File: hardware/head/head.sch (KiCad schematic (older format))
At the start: 12 parts, among them J1 DB9_Male, J2 Stats_Button, J3 Flush_Button, J4 Brew_Button, J5 Temp_Ok, J6 Display, J7 HX711, J8 Rotary_Encoder, U1 Teensy4.0

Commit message: Update head unit
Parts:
- removed H1: MountingHole_Pad, MountingHole:MountingHole_2.5mm_Pad, symbol Mechanical:MountingHole_Pad
- removed J4: Brew_Button, Connector_PinHeader_2.54mm:PinHeader_1x02_P2.54mm_Vertical, symbol Connector:Conn_01x02_Male
- added C1, C13, C14, C15: 0.1uF, Capacitor_THT:C_Disc_D5.1mm_W3.2mm_P5.00mm, symbol Device:C
- added C10, C12, C4, C6, C7, C9: 1nF, Capacitor_THT:C_Disc_D5.1mm_W3.2mm_P5.00mm, symbol Device:C
- added C11, C5, C8: 10nF, Capacitor_THT:C_Disc_D5.1mm_W3.2mm_P5.00mm, symbol Device:C
- added C2: 150uF, Capacitor_THT:CP_Radial_D5.0mm_P2.00mm, symbol Device:CP
- added C3: 100uF, Capacitor_THT:CP_Radial_D5.0mm_P2.00mm, symbol Device:CP
- added D1: 1N5817, Diode_THT:D_DO-41_SOD81_P10.16mm_Horizontal, symbol Diode:1N5817
- added H3, H4: MountingHole_Pad, MountingHole:MountingHole_2.5mm_Pad, symbol Mechanical:MountingHole_Pad
- added J10: Pump_Active, Connector_PinHeader_2.54mm:PinHeader_1x02_P2.54mm_Vertical, symbol Connector:Conn_01x02_Male
- added J4: Brew_Button, Connector_PinHeader_2.54mm:PinHeader_1x04_P2.54mm_Vertical, symbol Connector:Conn_01x04_Male
- added J9: Heater_Active, Connector_PinHeader_2.54mm:PinHeader_1x02_P2.54mm_Vertical, symbol Connector:Conn_01x02_Male
- added L1: 22uH, Inductor_THT:L_Axial_L11.0mm_D4.5mm_P15.24mm_Horizontal_Fastron_MECC, symbol Device:L
- added Q1: IRF540N, Package_TO_SOT_THT:TO-220-3_Vertical, symbol Transistor_FET:IRF540N
- added R10, R5, R6, R7, R8, R9: 10k, Resistor_THT:R_Axial_DIN0204_L3.6mm_D1.6mm_P5.08mm_Horizontal, symbol Device:R
- added R11, R12: 400, Resistor_THT:R_Axial_DIN0204_L3.6mm_D1.6mm_P5.08mm_Horizontal, symbol Device:R
- added R13: 650, Resistor_THT:R_Axial_DIN0204_L3.6mm_D1.6mm_P5.08mm_Horizontal, symbol Device:R
- added R14, R15: 220, Resistor_THT:R_Axial_DIN0204_L3.6mm_D1.6mm_P5.08mm_Horizontal, symbol Device:R
- added R2, R3, R4: 1M, Resistor_THT:R_Axial_DIN0204_L3.6mm_D1.6mm_P5.08mm_Horizontal, symbol Device:R
- added U2: MAX757, Package_DIP:DIP-8_W7.62mm, symbol boost_converter:MAX757
- added U3, U4, U5: INA126, Package_DIP:DIP-8_W7.62mm, symbol Amplifier_Instrumentation:INA128
- J7: value HX711 -> Load_Cell; footprint Connector_RJ:RJ14_Connfly_DS1133-S4_Horizontal -> Connector_PinHeader_2.54mm:PinHeader_1x04_P2.54mm_Vertical
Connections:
- net +3V3: now also C13.1, C14.1, C15.1, C2.1, L1.1, U2.1 (~SHDN), U2.5 (LBI), U3.7 (V+), U4.7 (V+), U5.7 (V+); no longer J1.2
- net BREW_BUTTON: now also J4.3 (Pin_3)
- net GND: now also J1.2, J1.4, C1.2, C10.1, C12.2, C13.2, C14.2, C15.2, C2.2, C3.2, C4.1, C6.2, C7.1, C9.2, H3.1, H4.1, J4.1 (Pin_1), J4.2 (Pin_2), R14.2, R15.2, R2.2, R3.2, R4.2, U2.2 (3/~5), U2.7 (GND), U3.4 (V-), U3.5 (Ref), U4.4 (V-), U4.5 (Ref), U5.4 (V-), U5.5 (Ref); no longer J1.1
- net TEMP_OK: now also U1.11 (9_OUT1C); no longer U1.12 (10_CS_MQSR)
- net BOILER_BOTTOM_TEMP+: now reaches J1.7
- net BOILER_BOTTOM_TEMP+: now also R7.1
- net BOILER_BOTTOM_TEMP-: now reaches J1.8
- net BOILER_BOTTOM_TEMP-: now also R3.1, R8.1
- net SCALE_OUT: now reaches U1.23 (16_A2_RX4_SCL1)
- net SCALE_OUT: now also U5.6
- net GROUPHEAD_TEMP renamed BOILER_TOP_TEMP
- net BOILER_TOP_TEMP: now also U3.6; no longer J1.4
- net HEATER_RELAY: no longer names the net of U1.14 (12_MISO_MQSL)
- net HEATER_RELAY: no longer J1.6
- net HX711_DT renamed BREW_READY
- net BREW_READY: now also Q1.1 (G); no longer J7.3 (Pin_3)
- net HX711_SCK renamed LOAD_CELL-
- net LOAD_CELL-: now also R10.1, R4.1; no longer U1.11 (9_OUT1C)
- net PUMP renamed BOILER_TOP_TEMP+
- net BOILER_TOP_TEMP+: now also R5.1; no longer U1.13 (11_MOSI_CTX1)
- net PUMP_TEMP renamed BOILER_BOTTOM_TEMP
- net BOILER_BOTTOM_TEMP: now also U4.6; no longer J1.3
- new net: R12.1, U4.1 (Rg)
- new net: C8.2, C9.1, R8.2, U4.2 (-)
- new net: C7.2, C8.1, R7.2, U4.3 (+)
- new net: R12.2, U4.8 (Rg)
- new net: R11.1, U3.1 (Rg)
- new net: C5.2, C6.1, R6.2, U3.2 (-)
- new net: C4.2, C5.1, R5.2, U3.3 (+)
- new net: R11.2, U3.8 (Rg)
- new net: R13.1, U5.1 (Rg)
- new net: C11.2, C12.1, R10.2, U5.2 (-)
- new net: C10.2, C11.1, R9.2, U5.3 (+)
- new net: R13.2, U5.8 (Rg)
- new net: C1.1, U2.3 (REF)
- new net: D1.2 (A), L1.2, U2.8 (LX)
- new net: J4.4 (Pin_4), Q1.3 (S)
- new net: J9.2 (Pin_2), R14.1
- new net: J10.2 (Pin_2), R15.1
- new net +5V: C3.1, D1.1 (K), Q1.2 (D), U2.6 (OUT)
- new net BOILER_TOP_TEMP-: J1.6, R2.1, R6.1
- new net HEATER_SSR+: J1.1, J9.1 (Pin_1), U1.13 (11_MOSI_CTX1)
- new net LOAD_CELL+: J7.3 (Pin_3), R9.1
- new net PUMP_SSR+: J1.3, J10.1 (Pin_1), U1.12 (10_CS_MQSR)
- no-connect marks 37 -> 16
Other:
- moved on the sheet: J2, J5, J6, J7, J8, R1, U1

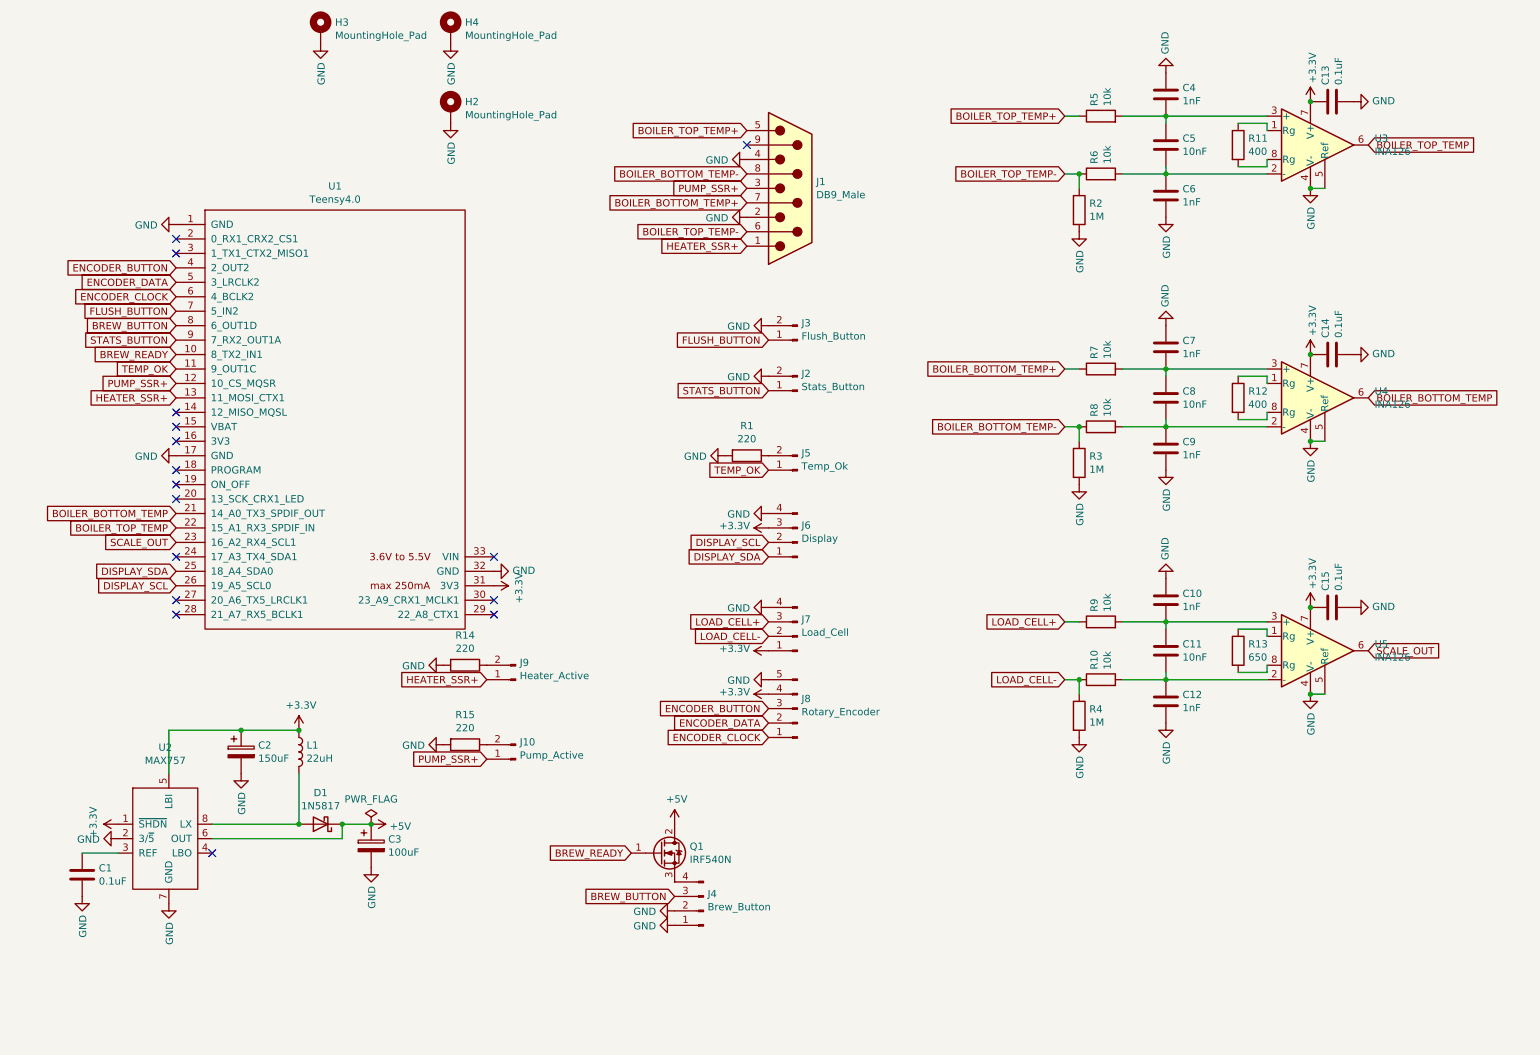
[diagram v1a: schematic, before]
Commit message: Reorder caps and resistors
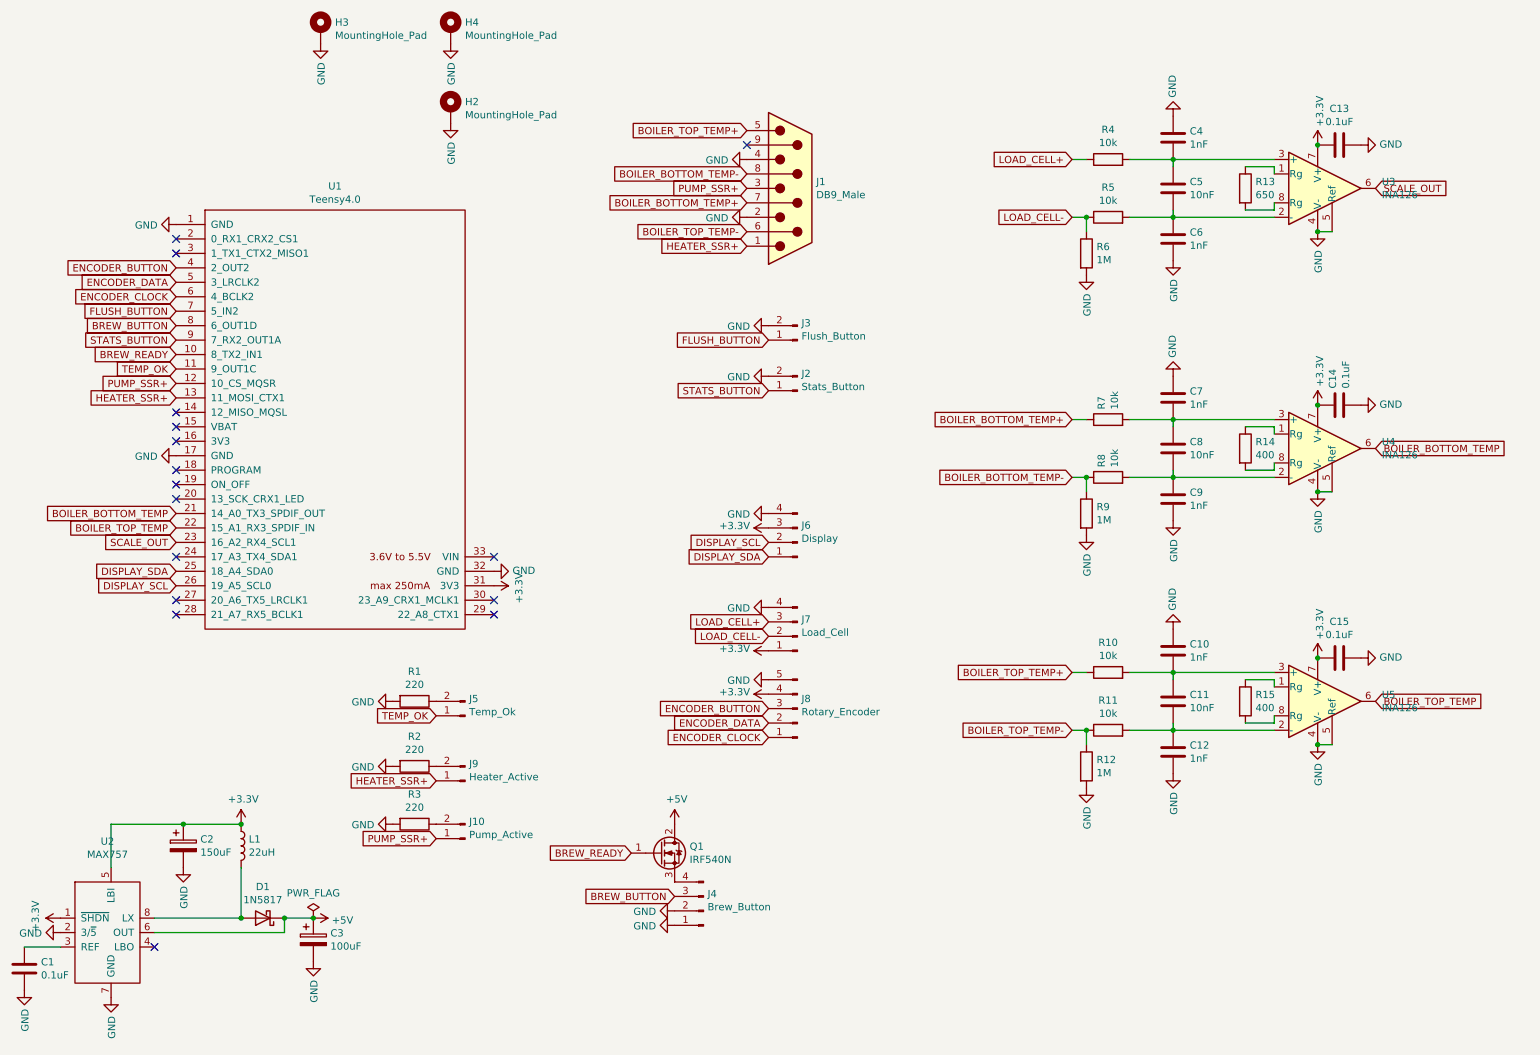
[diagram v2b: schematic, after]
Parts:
- renumbered C4 to C10, C5 to C11, C6 to C12, C15 to C13, C13 to C15, C10 to C4, C11 to C5, C12 to C6, R5 to R10, R6 to R11, R2 to R12, R12 to R14, R11 to R15, R14 to R2, R15 to R3, R9 to R4, R10 to R5, R4 to R6, R3 to R9, U5 to U3, U3 to U5
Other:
- moved on the sheet: C1, C10, C11, C12, C13, C14, C15, C2, C3, C4, C5, C6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

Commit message: Vias for days
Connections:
- net +5V: now also J4.2 (Pin_2); no longer Q1.2 (D)
- net BREW_BUTTON: now also J4.4 (Pin_4); no longer J4.3 (Pin_3)
- net GND: now also J4.3 (Pin_3), Q1.3 (S); no longer J4.1 (Pin_1), J4.2 (Pin_2)
- new net: J4.1 (Pin_1), Q1.2 (D)
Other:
- moved on the sheet: Q1
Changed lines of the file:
@@
 Connection ~ 2850 6800
-$Comp
-L Transistor_FET:IRF540N Q1
-U 1 1 60728D2B
-P 5250 6350
-F 0 "Q1" H 5454 6396 50  0000 L CNN
-F 1 "IRF540N" H 5454 6305 50  0000 L CNN
-F 2 "Package_TO_SOT_THT:TO-220-3_Vertical" H 5500 6275 50  0001 L CIN
-F 3 "http://www.irf.com/product-info/datasheets/data/irf540n.pdf" H 5250 6350 50  0001 L CNN
-	1    5250 6350
-	1    0    0    -1
-$EndComp
-Text GLabel 5050 6350 0    50   Input ~ 0
-BREW_READY
 $Comp
 L power:+5V #PWR016
 U 1 1 6072C196
-P 5350 6150
-F 0 "#PWR016" H 5350 6000 50  0001 C CNN
-F 1 "+5V" H 5365 6323 50  0000 C CNN
-F 2 "" H 5350 6150 50  0001 C CNN
-F 3 "" H 5350 6150 50  0001 C CNN
-	1    5350 6150
-	1    0    0    -1
-$EndComp
-$Comp
-L Connector:Conn_01x04_Male J4
-U 1 1 6072E9C5
-P 5550 6750
-F 0 "J4" H 5522 6632 50  0000 R CNN
-F 1 "Brew_Button" H 5522 6723 50  0000 R CNN
-F 2 "Connector_PinHeader_2.54mm:PinHeader_1x04_P2.54mm_Vertical" H 5550 6750 50  0001 C CNN
-F 3 "~" H 5550 6750 50  0001 C CNN
-	1    5550 6750
-	-1   0    0    1
+P 5350 6750
+F 0 "#PWR016" H 5350 6600 50  0001 C CNN
+F 1 "+5V" H 5365 6923 50  0000 C CNN
+F 2 "" H 5350 6750 50  0001 C CNN
+F 3 "" H 5350 6750 50  0001 C CNN
+	1    5350 6750
+	0    -1   -1   0
 $EndComp
 $Comp
 L power:GND #PWR017
 U 1 1 6072F3F3
-P 5350 6750
-F 0 "#PWR017" H 5350 6500 50  0001 C CNN
-F 1 "GND" V 5355 6622 50  0000 R CNN
-F 2 "" H 5350 6750 50  0001 C CNN
-F 3 "" H 5350 6750 50  0001 C CNN
-	1    5350 6750
+P 5350 6650
+F 0 "#PWR017" H 5350 6400 50  0001 C CNN
+F 1 "GND" V 5355 6522 50  0000 R CNN
+F 2 "" H 5350 6650 50  0001 C CNN
+F 3 "" H 5350 6650 50  0001 C CNN
+	1    5350 6650
 	0    1    1    0
 $EndComp
-$Comp
-L power:GND #PWR018
-U 1 1 6072F88E
-P 5350 6850
-F 0 "#PWR018" H 5350 6600 50  0001 C CNN
-F 1 "GND" V 5355 6722 50  0000 R CNN
-F 2 "" H 5350 6850 50  0001 C CNN
-F 3 "" H 5350 6850 50  0001 C CNN
-	1    5350 6850
-	0    1    1    0
-$EndComp
-Text GLabel 5350 6650 0    50   Input ~ 0
+Text GLabel 5350 6550 0    50   Input ~ 0
 BREW_BUTTON
 Text GLabel 1900 2900 0    50   Input ~ 0
@@
 	1    0    0    -1
 $EndComp
+Text GLabel 5050 7050 0    50   Input ~ 0
+BREW_READY
+$Comp
+L Connector:Conn_01x04_Male J4
+U 1 1 6072E9C5
+P 5550 6750
+F 0 "J4" H 5522 6632 50  0000 R CNN
+F 1 "Brew_Button" H 5522 6723 50  0000 R CNN
+F 2 "Connector_PinHeader_2.54mm:PinHeader_1x04_P2.54mm_Vertical" H 5550 6750 50  0001 C CNN
+F 3 "~" H 5550 6750 50  0001 C CNN
+	1    5550 6750
+	-1   0    0    1
+$EndComp
+$Comp
+L power:GND #PWR018
+U 1 1 6072F88E
+P 5350 7250
+F 0 "#PWR018" H 5350 7000 50  0001 C CNN
+F 1 "GND" V 5355 7122 50  0000 R CNN
+F 2 "" H 5350 7250 50  0001 C CNN
+F 3 "" H 5350 7250 50  0001 C CNN
+	1    5350 7250
+	1    0    0    -1
+$EndComp
+$Comp
+L Transistor_FET:IRF540N Q1
+U 1 1 60728D2B
+P 5250 7050
+F 0 "Q1" H 5454 7096 50  0000 L CNN
+F 1 "IRF540N" H 5454 7005 50  0000 L CNN
+F 2 "Package_TO_SOT_THT:TO-220-3_Vertical" H 5500 6975 50  0001 L CIN
+F 3 "http://www.irf.com/product-info/datasheets/data/irf540n.pdf" H 5250 7050 50  0001 L CNN
+	1    5250 7050
+	1    0    0    -1
+$EndComp
